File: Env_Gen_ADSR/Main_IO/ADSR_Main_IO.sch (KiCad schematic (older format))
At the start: 27 parts, among them J1 Gate, J2 Trigger, J3 Env, J4 Conn_01x16, U1 AS3310, U2 TL071

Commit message: Fix envelope generator front panel size and alignment with IO board.
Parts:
- removed R10: 10K, Resistor_SMD:R_0805_2012Metric, symbol Device:R_US
- removed RV5: 100K, Potentiometer_THT:Potentiometer_Bourns_3296W_Vertical, symbol Device:R_POT_TRIM_US
- added D1: LED, Eurorack:LED_D5.0mm, symbol Device:LED
- added R12: R_US, Resistor_SMD:R_0805_2012Metric, symbol Device:R_US
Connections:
- net -12V: now also R12.2
- net at J3.T, R9.2, U1.2 (ENVOUT)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: now also D1.2 (A)
- new net: D1.1 (K), R12.1
- no-connect marks 2 -> 3
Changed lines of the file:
@@
 EESchema Schematic File Version 4
-LIBS:AS3310_ADSR_IO-cache
-EELAYER 29 0
+LIBS:ADSR_Main_IO-cache
+EELAYER 30 0
 EELAYER END
 $Descr A4 11693 8268
@@
 Wire Wire Line
 	7600 2350 7850 2350
-$Comp
-L Device:R_POT_TRIM_US RV5
-U 1 1 5D856871
-P 4450 1300
-F 0 "RV5" H 4383 1346 50  0000 R CNN
-F 1 "100K" H 4383 1255 50  0000 R CNN
-F 2 "Potentiometer_THT:Potentiometer_Bourns_3296W_Vertical" H 4450 1300 50  0001 C CNN
-F 3 "~" H 4450 1300 50  0001 C CNN
-	1    4450 1300
-	1    0    0    -1
-$EndComp
-$Comp
-L Device:R_US R10
-U 1 1 5D857C33
-P 4900 1300
-F 0 "R10" V 4695 1300 50  0000 C CNN
-F 1 "10K" V 4786 1300 50  0000 C CNN
-F 2 "Resistor_SMD:R_0805_2012Metric" V 4940 1290 50  0001 C CNN
-F 3 "~" H 4900 1300 50  0001 C CNN
-	1    4900 1300
-	0    1    1    0
-$EndComp
-$Comp
-L power:+12V #PWR0126
-U 1 1 5D8585A9
-P 4450 1050
-F 0 "#PWR0126" H 4450 900 50  0001 C CNN
-F 1 "+12V" H 4465 1223 50  0000 C CNN
-F 2 "" H 4450 1050 50  0001 C CNN
-F 3 "" H 4450 1050 50  0001 C CNN
-	1    4450 1050
-	1    0    0    -1
-$EndComp
-$Comp
-L power:GNDREF #PWR0127
-U 1 1 5D85899F
-P 4450 1550
-F 0 "#PWR0127" H 4450 1300 50  0001 C CNN
-F 1 "GNDREF" H 4455 1377 50  0001 C CNN
-F 2 "" H 4450 1550 50  0001 C CNN
-F 3 "" H 4450 1550 50  0001 C CNN
-	1    4450 1550
-	1    0    0    -1
-$EndComp
-Wire Wire Line
-	4450 1450 4450 1550
-Wire Wire Line
-	4450 1050 4450 1150
-Wire Wire Line
-	4600 1300 4750 1300
-Wire Wire Line
-	5050 1300 5150 1300
-Wire Wire Line
-	5150 1300 5150 2050
-Wire Wire Line
-	5150 2050 5300 2050
 Wire Wire Line
 	6300 3950 6300 2450
@@
 Wire Wire Line
 	8300 4350 8300 4400
+$Comp
+L Device:LED D1
+U 1 1 5D8B3156
+P 7600 3450
+F 0 "D1" V 7639 3333 50  0000 R CNN
+F 1 "LED" V 7548 3333 50  0000 R CNN
+F 2 "Eurorack:LED_D5.0mm" H 7600 3450 50  0001 C CNN
+F 3 "~" H 7600 3450 50  0001 C CNN
+	1    7600 3450
+	0    -1   -1   0
+$EndComp
+Wire Wire Line
+	7600 3300 7600 3100
+Connection ~ 7600 3100
+$Comp
+L Device:R_US R12
+U 1 1 5D8B8060
+P 7600 3950
+F 0 "R12" H 7668 3996 50  0000 L CNN
+F 1 "R_US" H 7668 3905 50  0000 L CNN
+F 2 "Resistor_SMD:R_0805_2012Metric" V 7640 3940 50  0001 C CNN
+F 3 "~" H 7600 3950 50  0001 C CNN
+	1    7600 3950
+	1    0    0    -1
+$EndComp
+Wire Wire Line
+	7600 3600 7600 3800
+$Comp
+L power:-12V #PWR0131
+U 1 1 5D8BBDA9
+P 7600 4200
+F 0 "#PWR0131" H 7600 4300 50  0001 C CNN
+F 1 "-12V" H 7615 4373 50  0000 C CNN
+F 2 "" H 7600 4200 50  0001 C CNN
+F 3 "" H 7600 4200 50  0001 C CNN
+	1    7600 4200
+	-1   0    0    1
+$EndComp
+Wire Wire Line
+	7600 4200 7600 4100
+NoConn ~ 5300 2050
 $EndSCHEMATC

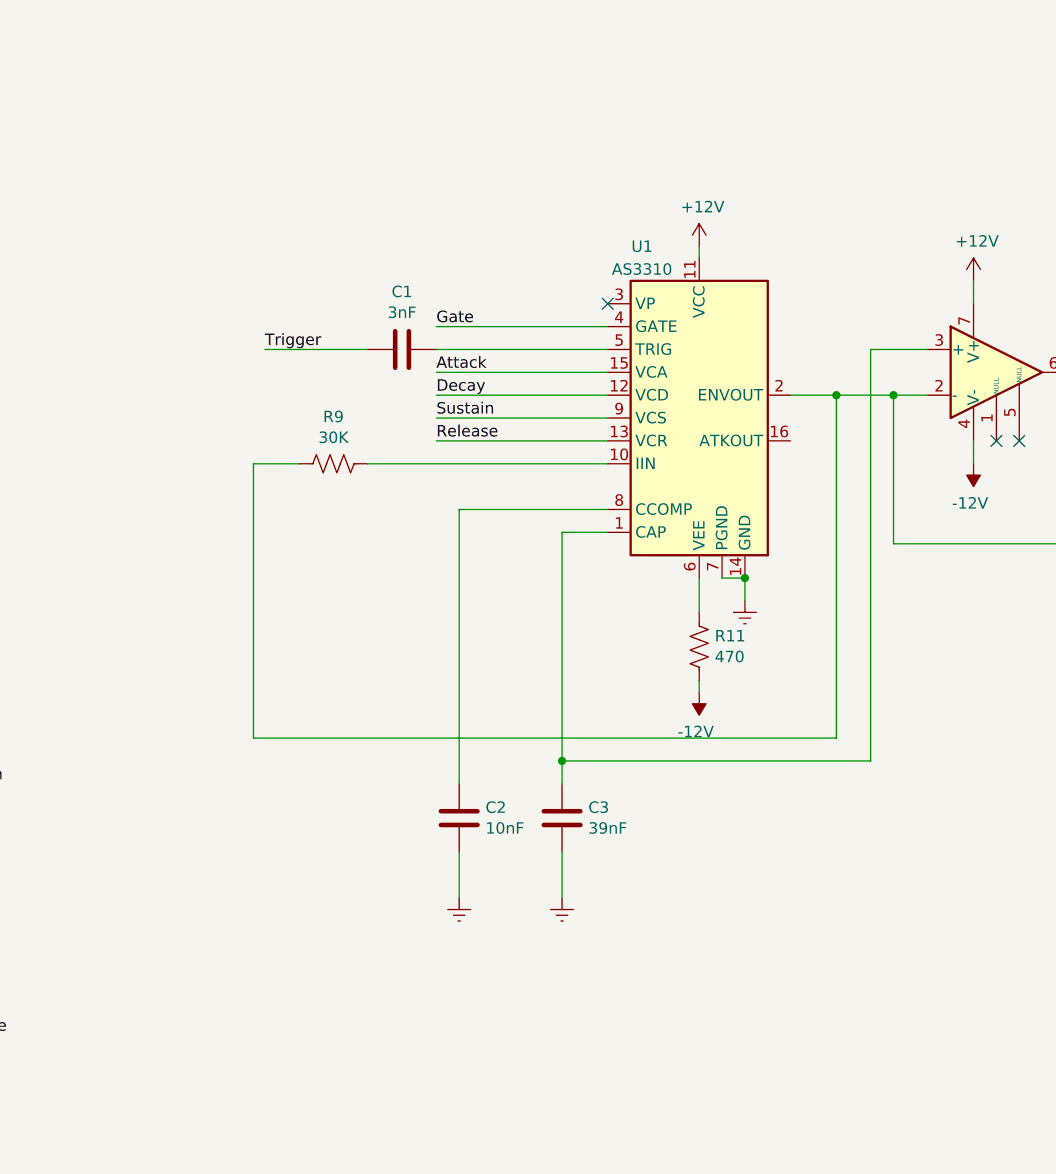
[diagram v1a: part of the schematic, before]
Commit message: Clean up envelope gen board
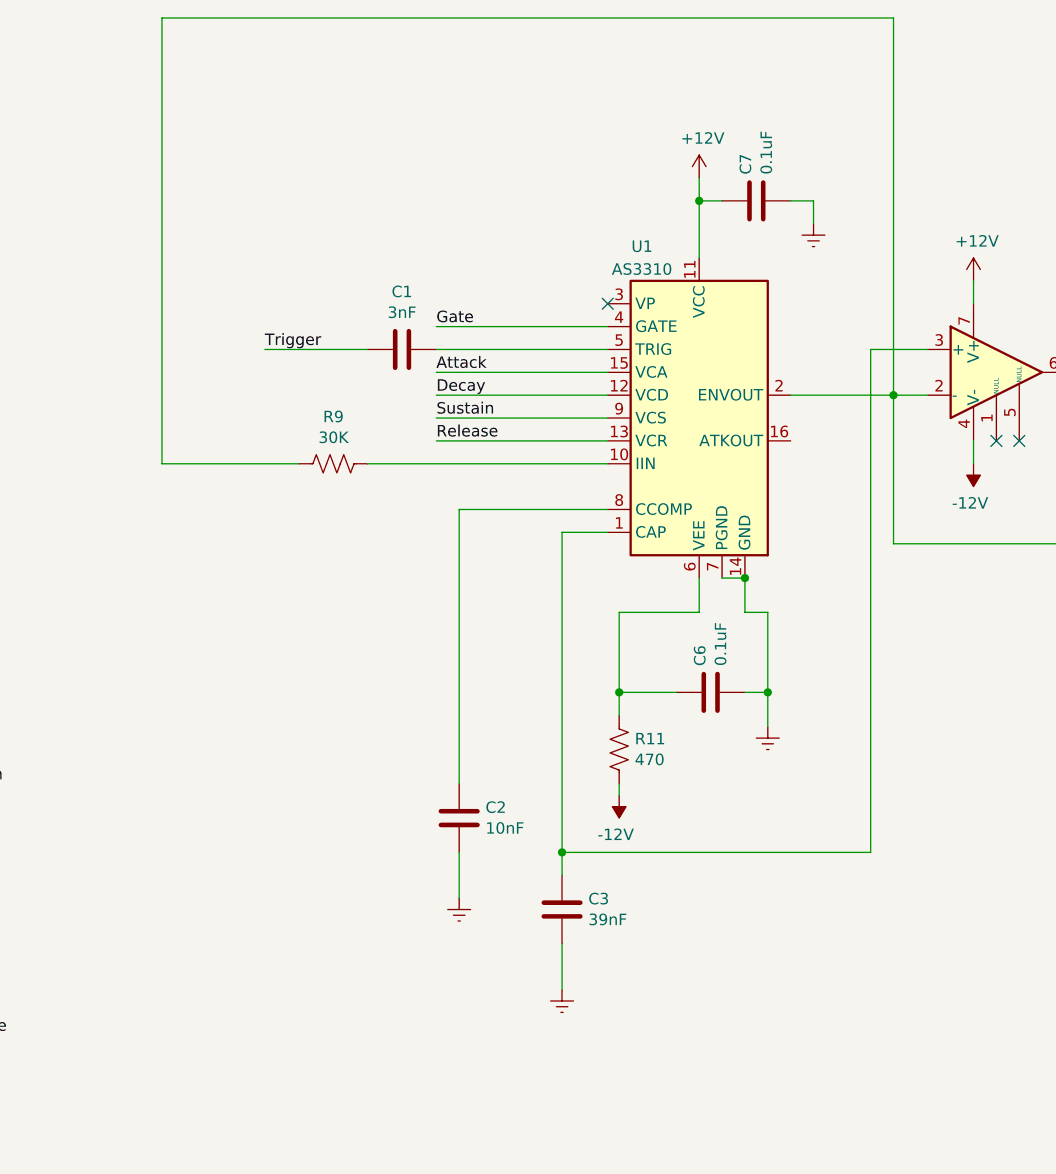
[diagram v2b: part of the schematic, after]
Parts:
- added C6, C7: 0.1uF, Capacitor_SMD:C_0805_2012Metric, symbol Device:C
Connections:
- net +12V: now also C7.1
- net GNDREF: now also C6.2, C7.2
- net at R11.1, U1.6 (VEE): now also C6.1
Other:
- moved on the sheet: C3, R11
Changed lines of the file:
@@
 L power:+12V #PWR0118
 U 1 1 5D815D74
-P 5700 1800
-F 0 "#PWR0118" H 5700 1650 50  0001 C CNN
-F 1 "+12V" H 5715 1973 50  0000 C CNN
-F 2 "" H 5700 1800 50  0001 C CNN
-F 3 "" H 5700 1800 50  0001 C CNN
-	1    5700 1800
+P 5700 1500
+F 0 "#PWR0118" H 5700 1350 50  0001 C CNN
+F 1 "+12V" H 5715 1673 50  0000 C CNN
+F 2 "" H 5700 1500 50  0001 C CNN
+F 3 "" H 5700 1500 50  0001 C CNN
+	1    5700 1500
 	1    0    0    -1
 $EndComp
@@
 L power:-12V #PWR0119
 U 1 1 5D816116
-P 5700 3750
-F 0 "#PWR0119" H 5700 3850 50  0001 C CNN
-F 1 "-12V" H 5715 3923 50  0000 C CNN
-F 2 "" H 5700 3750 50  0001 C CNN
-F 3 "" H 5700 3750 50  0001 C CNN
-	1    5700 3750
+P 5350 4200
+F 0 "#PWR0119" H 5350 4300 50  0001 C CNN
+F 1 "-12V" H 5365 4373 50  0000 C CNN
+F 2 "" H 5350 4200 50  0001 C CNN
+F 3 "" H 5350 4200 50  0001 C CNN
+	1    5350 4200
 	-1   0    0    1
 $EndComp
@@
 L power:GNDREF #PWR0120
 U 1 1 5D8163F7
-P 5900 3350
-F 0 "#PWR0120" H 5900 3100 50  0001 C CNN
-F 1 "GNDREF" H 5905 3177 50  0001 C CNN
-F 2 "" H 5900 3350 50  0001 C CNN
-F 3 "" H 5900 3350 50  0001 C CNN
-	1    5900 3350
+P 6000 3900
+F 0 "#PWR0120" H 6000 3650 50  0001 C CNN
+F 1 "GNDREF" H 6005 3727 50  0001 C CNN
+F 2 "" H 6000 3900 50  0001 C CNN
+F 3 "" H 6000 3900 50  0001 C CNN
+	1    6000 3900
 	1    0    0    -1
 $EndComp
 Wire Wire Line
 	5800 3250 5900 3250
-Wire Wire Line
-	5900 3250 5900 3350
 Connection ~ 5900 3250
 $Comp
 L Device:R_US R11
 U 1 1 5D81B50C
-P 5700 3550
-F 0 "R11" H 5768 3596 50  0000 L CNN
-F 1 "470" H 5768 3505 50  0000 L CNN
-F 2 "Resistor_SMD:R_0805_2012Metric" V 5740 3540 50  0001 C CNN
-F 3 "~" H 5700 3550 50  0001 C CNN
-	1    5700 3550
+P 5350 4000
+F 0 "R11" H 5418 4046 50  0000 L CNN
+F 1 "470" H 5418 3955 50  0000 L CNN
+F 2 "Resistor_SMD:R_0805_2012Metric" V 5390 3990 50  0001 C CNN
+F 3 "~" H 5350 4000 50  0001 C CNN
+	1    5350 4000
 	1    0    0    -1
 $EndComp
@@
 	5700 3250 5700 3400
 Wire Wire Line
-	5700 3700 5700 3750
+	5350 4150 5350 4200
 $Comp
 L Device:C C3
 U 1 1 5D820825
-P 5100 4300
-F 0 "C3" H 5215 4346 50  0000 L CNN
-F 1 "39nF" H 5215 4255 50  0000 L CNN
-F 2 "Capacitor_SMD:C_0805_2012Metric" H 5138 4150 50  0001 C CNN
-F 3 "~" H 5100 4300 50  0001 C CNN
-	1    5100 4300
+P 5100 4700
+F 0 "C3" H 5215 4746 50  0000 L CNN
+F 1 "39nF" H 5215 4655 50  0000 L CNN
+F 2 "Capacitor_SMD:C_0805_2012Metric" H 5138 4550 50  0001 C CNN
+F 3 "~" H 5100 4700 50  0001 C CNN
+	1    5100 4700
 	1    0    0    -1
 $EndComp
@@
 L power:GNDREF #PWR0122
 U 1 1 5D827CC0
-P 5100 4650
-F 0 "#PWR0122" H 5100 4400 50  0001 C CNN
-F 1 "GNDREF" H 5105 4477 50  0001 C CNN
-F 2 "" H 5100 4650 50  0001 C CNN
-F 3 "" H 5100 4650 50  0001 C CNN
-	1    5100 4650
-	1    0    0    -1
-$EndComp
-Wire Wire Line
-	5100 4650 5100 4450
+P 5100 5050
+F 0 "#PWR0122" H 5100 4800 50  0001 C CNN
+F 1 "GNDREF" H 5105 4877 50  0001 C CNN
+F 2 "" H 5100 5050 50  0001 C CNN
+F 3 "" H 5100 5050 50  0001 C CNN
+	1    5100 5050
+	1    0    0    -1
+$EndComp
+Wire Wire Line
+	5100 5050 5100 4850
 $Comp
 L Device:R_US R9
@@
 Wire Wire Line
 	4250 2750 5300 2750
-Wire Wire Line
-	6100 2450 6300 2450
 NoConn ~ 7000 2650
 NoConn ~ 7100 2650
-Wire Wire Line
-	5700 1800 5700 1850
 $Comp
 L power:+12V #PWR0123
@@
 	4650 2950 4650 4150
 Wire Wire Line
-	5100 3050 5100 4050
-Wire Wire Line
-	5100 4050 6450 4050
-Wire Wire Line
-	6450 4050 6450 2250
+	5100 3050 5100 4450
+Wire Wire Line
+	5100 4450 6450 4450
+Wire Wire Line
+	6450 4450 6450 2250
 Wire Wire Line
 	6450 2250 6700 2250
-Connection ~ 5100 4050
-Wire Wire Line
-	5100 4050 5100 4150
+Wire Wire Line
+	5100 4450 5100 4550
 Wire Wire Line
 	7300 2350 7600 2350
@@
 Wire Wire Line
 	7600 2350 7850 2350
-Wire Wire Line
-	6300 3950 6300 2450
-Connection ~ 6300 2450
-Wire Wire Line
-	6300 2450 6550 2450
-Wire Wire Line
-	3950 2750 3750 2750
-Wire Wire Line
-	3750 2750 3750 3950
-Wire Wire Line
-	3750 3950 6300 3950
 $Comp
 L Device:CP1 C4
@@
 	7600 4200 7600 4100
 NoConn ~ 5300 2050
+$Comp
+L Device:C C7
+U 1 1 5D9DDA40
+P 5950 1600
+F 0 "C7" H 6065 1646 50  0000 L CNN
+F 1 "0.1uF" H 6065 1555 50  0000 L CNN
+F 2 "Capacitor_SMD:C_0805_2012Metric" H 5988 1450 50  0001 C CNN
+F 3 "~" H 5950 1600 50  0001 C CNN
+	1    5950 1600
+	0    -1   -1   0
+$EndComp
+Wire Wire Line
+	5700 1500 5700 1600
+Wire Wire Line
+	5700 1600 5800 1600
+Connection ~ 5700 1600
+Wire Wire Line
+	5700 1600 5700 1850
+Wire Wire Line
+	6100 2450 6550 2450
+Wire Wire Line
+	6550 2450 6550 800
+Wire Wire Line
+	6550 800  3350 800
+Wire Wire Line
+	3350 800  3350 2750
+Wire Wire Line
+	3350 2750 3950 2750
+$Comp
+L power:GNDREF #PWR0126
+U 1 1 5DA0A54B
+P 6200 1700
+F 0 "#PWR0126" H 6200 1450 50  0001 C CNN
+F 1 "GNDREF" H 6205 1527 50  0001 C CNN
+F 2 "" H 6200 1700 50  0001 C CNN
+F 3 "" H 6200 1700 50  0001 C CNN
+	1    6200 1700
+	1    0    0    -1
+$EndComp
+Wire Wire Line
+	6100 1600 6200 1600
+Wire Wire Line
+	6200 1600 6200 1700
+Connection ~ 5100 4450
+$Comp
+L Device:C C6
+U 1 1 5DA174F0
+P 5750 3750
+F 0 "C6" H 5865 3796 50  0000 L CNN
+F 1 "0.1uF" H 5865 3705 50  0000 L CNN
+F 2 "Capacitor_SMD:C_0805_2012Metric" H 5788 3600 50  0001 C CNN
+F 3 "~" H 5750 3750 50  0001 C CNN
+	1    5750 3750
+	0    -1   -1   0
+$EndComp
+Wire Wire Line
+	5350 3850 5350 3750
+Wire Wire Line
+	5350 3400 5700 3400
+Wire Wire Line
+	5350 3750 5600 3750
+Connection ~ 5350 3750
+Wire Wire Line
+	5350 3750 5350 3400
+Wire Wire Line
+	5900 3750 6000 3750
+Wire Wire Line
+	6000 3750 6000 3900
+Wire Wire Line
+	6000 3750 6000 3400
+Wire Wire Line
+	6000 3400 5900 3400
+Wire Wire Line
+	5900 3250 5900 3400
+Connection ~ 6000 3750
 $EndSCHEMATC

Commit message: Fix resistor values for ADSR Sustain
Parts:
- R5: value R_US -> 22K
- R6: value R_US -> 16K

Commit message: Fix backwards knobs
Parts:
- removed C4, C5: CP1, Capacitor_SMD:CP_Elec_4x3, symbol Device:CP1
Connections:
- net +12V: now also RV3.3; no longer RV3.1
- net -12V: now also RV1.3, RV2.3, RV4.3; no longer RV1.1, RV2.1, RV4.1
- net GNDREF: now also RV1.1, RV2.1, RV3.1, RV4.1; no longer RV1.3, RV2.3, RV3.3, RV4.3
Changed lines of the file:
@@
 F 3 "~" H 1550 1600 50  0001 C CNN
 	1    1550 1600
-	1    0    0    -1
+	1    0    0    1
 $EndComp
 $Comp
@@
 F 3 "~" H 1550 2700 50  0001 C CNN
 	1    1550 2700
-	1    0    0    -1
+	1    0    0    1
 $EndComp
 $Comp
@@
 F 3 "~" H 1550 3800 50  0001 C CNN
 	1    1550 3800
-	1    0    0    -1
+	1    0    0    1
 $EndComp
 $Comp
@@
 F 3 "~" H 1550 4900 50  0001 C CNN
 	1    1550 4900
-	1    0    0    -1
+	1    0    0    1
 $EndComp
 $Comp
@@
 	7600 2350 7850 2350
 $Comp
-L Device:CP1 C4
-U 1 1 5D86C2D5
-P 8300 4550
-F 0 "C4" H 8415 4596 50  0000 L CNN
-F 1 "CP1" H 8415 4505 50  0000 L CNN
-F 2 "Capacitor_SMD:CP_Elec_4x3" H 8300 4550 50  0001 C CNN
-F 3 "~" H 8300 4550 50  0001 C CNN
-	1    8300 4550
-	1    0    0    -1
-$EndComp
-$Comp
-L Device:CP1 C5
-U 1 1 5D86C770
-P 8300 4950
-F 0 "C5" H 8415 4996 50  0000 L CNN
-F 1 "CP1" H 8415 4905 50  0000 L CNN
-F 2 "Capacitor_SMD:CP_Elec_4x3" H 8300 4950 50  0001 C CNN
-F 3 "~" H 8300 4950 50  0001 C CNN
-	1    8300 4950
-	1    0    0    -1
-$EndComp
-$Comp
-L power:GNDREF #PWR0128
-U 1 1 5D86CF5F
-P 8650 4750
-F 0 "#PWR0128" H 8650 4500 50  0001 C CNN
-F 1 "GNDREF" H 8655 4577 50  0001 C CNN
-F 2 "" H 8650 4750 50  0001 C CNN
-F 3 "" H 8650 4750 50  0001 C CNN
-	1    8650 4750
-	1    0    0    -1
-$EndComp
-Wire Wire Line
-	8300 4700 8300 4750
-Wire Wire Line
-	8300 4750 8650 4750
-Connection ~ 8300 4750
-Wire Wire Line
-	8300 4750 8300 4800
-$Comp
-L power:-12V #PWR0129
-U 1 1 5D872AB8
-P 8300 5150
-F 0 "#PWR0129" H 8300 5250 50  0001 C CNN
-F 1 "-12V" H 8315 5323 50  0000 C CNN
-F 2 "" H 8300 5150 50  0001 C CNN
-F 3 "" H 8300 5150 50  0001 C CNN
-	1    8300 5150
-	-1   0    0    1
-$EndComp
-Wire Wire Line
-	8300 5100 8300 5150
-$Comp
-L power:+12V #PWR0130
-U 1 1 5D875BA7
-P 8300 4350
-F 0 "#PWR0130" H 8300 4200 50  0001 C CNN
-F 1 "+12V" H 8315 4523 50  0000 C CNN
-F 2 "" H 8300 4350 50  0001 C CNN
-F 3 "" H 8300 4350 50  0001 C CNN
-	1    8300 4350
-	1    0    0    -1
-$EndComp
-Wire Wire Line
-	8300 4350 8300 4400
-$Comp
 L Device:LED D1
